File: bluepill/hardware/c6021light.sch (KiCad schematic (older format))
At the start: 77 parts, among them J1 Barrel_Jack_Switch, J10 Conn_01x02, J11 Conn_01x02, J12 XpressNet, J2 Conn_02x04_Odd_Even, J3 Conn_02x16_Row_Letter_First, J30 Loconet, J31 Conn_01x02, J32 Conn_01x02, J4 Conn_01x02, J5 Grove I2C, J50 USB_B_Micro, J51 Conn_01x06, J52 Debug UART, J6 Conn_01x02, J7 Conn_01x02, J8 RJ45, Q30 BC337, Q31 BC547, Q32 BC547, SW1 SW_Push, U1 L7805, U10 SN75176, U2 L7808, U3 MCP2562, U30 LM393, U4 ISO1050DUB, U50 CH340C

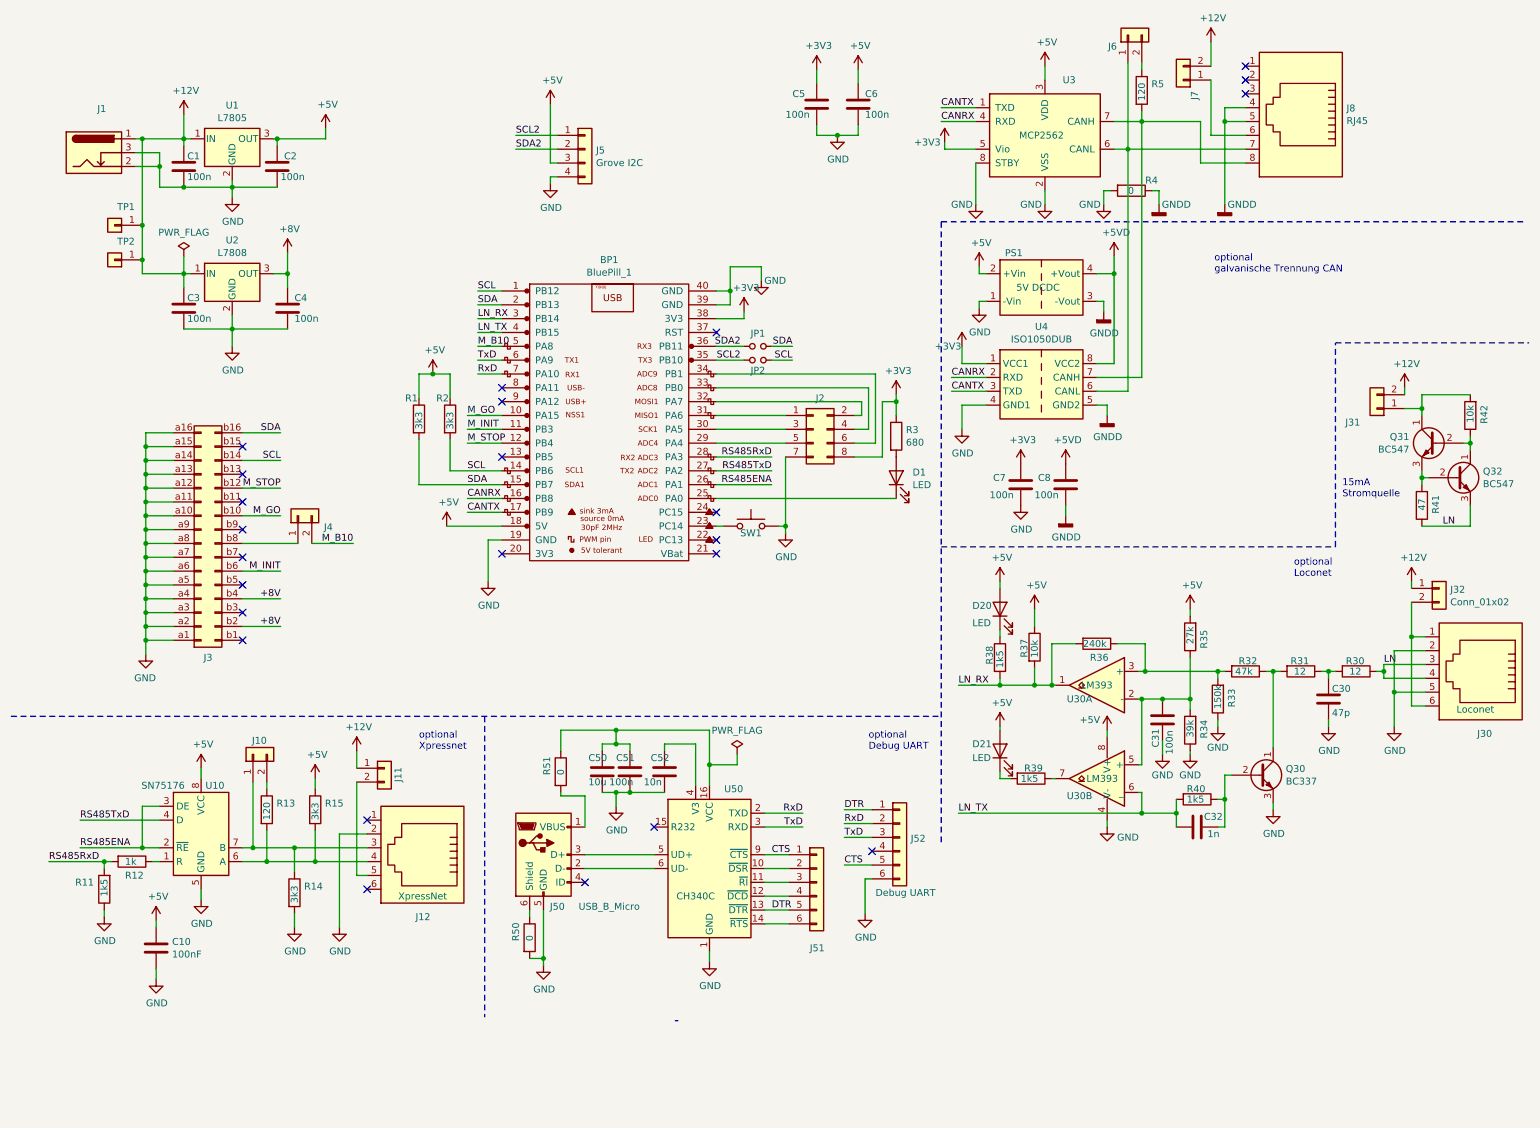
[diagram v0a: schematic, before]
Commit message: new PCB version 1.1. aka 2020/08 with some small fixes
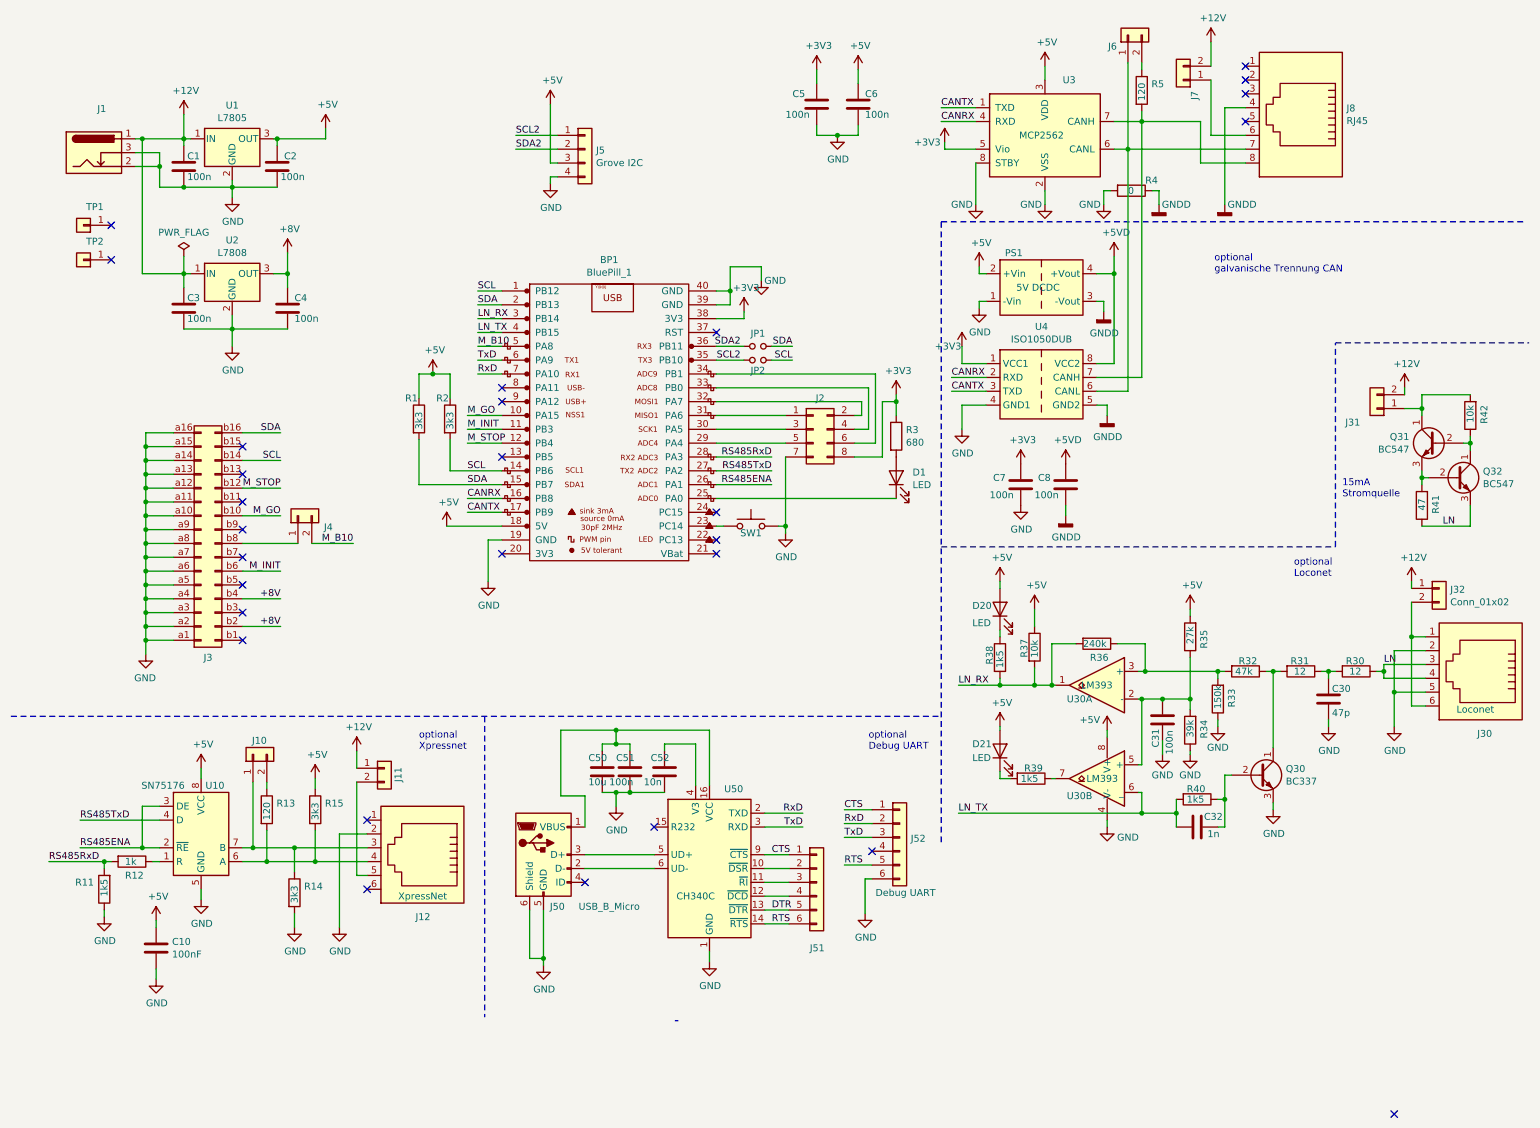
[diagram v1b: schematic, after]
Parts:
- removed R50, R51: 0, Resistor_SMD:R_1206_3216Metric_Pad1.42x1.75mm_HandSolder, symbol Device:R
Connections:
- net +12V: no longer TP1.1 (Pin_1), TP2.1 (Pin_1)
- net CTS: now also J52.1 (Pin_1); no longer J52.5 (Pin_5)
- net DTR: no longer J52.1 (Pin_1)
- net GND: now also J50.6 (Shield)
- net GNDD: no longer J8.5
- net RTS: now reaches J51.6 (Pin_6), U50.14 (~RTS)
- net RTS: now also J52.5 (Pin_5)
- net at C50.1, C51.1, U50.16 (VCC): now also J50.1 (VBUS)
- no-connect marks 24 -> 28
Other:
- moved on the sheet: TP1, TP2
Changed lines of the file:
@@
 Sheet 1 1
 Title "C6021 Light"
-Date "2020-06-09"
-Rev "1.0"
+Date "2020-08-03"
+Rev "1.1"
 Comp "Damian Philipp / Gerhard Bertelsmann"
 Comment1 ""
@@
 	7725 900  7725 1000
 $Comp
-L Connector:RJ45 J8
-U 1 1 5EDB2E8F
-P 9575 1200
-F 0 "J8" H 9245 1204 50  0000 R CNN
-F 1 "RJ45" H 9245 1295 50  0000 R CNN
-F 2 "w_conn_pc:mebp8" V 9575 1225 50  0001 C CNN
-F 3 "~" V 9575 1225 50  0001 C CNN
-	1    9575 1200
-	-1   0    0    1
-$EndComp
-$Comp
 L Device:C C5
 U 1 1 5EDB8D27
@@
 Wire Wire Line
 	9175 1200 9025 1200
-Wire Wire Line
-	9175 1300 9025 1300
 Wire Wire Line
 	9175 1400 8925 1400
@@
 Wire Wire Line
 	8175 5700 8175 5750
-$Comp
-L Device:R R50
-U 1 1 60480953
-P 4000 7200
-F 0 "R50" V 3900 7175 50  0000 L CNN
-F 1 "0" V 4000 7175 50  0000 L CNN
-F 2 "Resistor_SMD:R_1206_3216Metric_Pad1.42x1.75mm_HandSolder" V 3930 7200 50  0001 C CNN
-F 3 "~" H 4000 7200 50  0001 C CNN
-	1    4000 7200
-	1    0    0    -1
-$EndComp
 Wire Wire Line
 	4000 7350 4100 7350
@@
 Wire Wire Line
 	4100 7350 4100 7400
-Wire Wire Line
-	4000 7000 4000 7050
 $Comp
 L Device:C C51
@@
 Wire Wire Line
 	4625 5800 4625 5700
-Wire Wire Line
-	5300 5700 5300 5950
 Connection ~ 4625 5800
 Wire Wire Line
@@
 Wire Wire Line
 	5200 6100 5200 5800
-$Comp
-L Device:R R51
-U 1 1 6058F371
-P 4225 6000
-F 0 "R51" V 4125 5975 50  0000 L CNN
-F 1 "0" V 4225 5975 50  0000 L CNN
-F 2 "Resistor_SMD:R_1206_3216Metric_Pad1.42x1.75mm_HandSolder" V 4155 6000 50  0001 C CNN
-F 3 "~" H 4225 6000 50  0001 C CNN
-	1    4225 6000
-	1    0    0    -1
-$EndComp
-Wire Wire Line
-	4225 5850 4225 5700
 Wire Wire Line
 	4225 5700 4625 5700
@@
 Wire Wire Line
 	6475 6275 6275 6275
-Text Label 6275 6275 0    50   ~ 0
-DTR
 Wire Wire Line
 	6475 6675 6275 6675
-Text Label 6275 6675 0    50   ~ 0
-CTS
 NoConn ~ 6475 6575
 Wire Notes Line
@@
 	8925 1400 8925 1000
 Wire Wire Line
-	9025 1300 9025 1900
-Wire Wire Line
 	8325 1500 9175 1500
-Wire Wire Line
-	9025 1300 9025 1200
-Connection ~ 9025 1300
 Wire Notes Line
 	6975 2025 11200 2025
@@
 Text Notes 8950 2400 0    50   ~ 0
 optional\ngalvanische Trennung CAN
-Wire Wire Line
-	4225 6150 4225 6175
 Wire Wire Line
 	4225 6175 4400 6175
@@
 	1    0    0    -1
 $EndComp
-$Comp
-L power:PWR_FLAG #FLG0103
-U 1 1 60D33B68
-P 5500 5875
-F 0 "#FLG0103" H 5500 5950 50  0001 C CNN
-F 1 "PWR_FLAG" H 5500 6048 50  0000 C CNN
-F 2 "" H 5500 5875 50  0001 C CNN
-F 3 "~" H 5500 5875 50  0001 C CNN
-	1    5500 5875
-	1    0    0    -1
-$EndComp
-Wire Wire Line
-	5300 5950 5500 5950
-Wire Wire Line
-	5500 5950 5500 5875
-Connection ~ 5300 5950
-Wire Wire Line
-	5300 5950 5300 6100
 $Comp
 L Connector_Generic:Conn_01x04 J5
@@
 	1150 1425 1200 1425
 Wire Wire Line
-	1200 1425 1200 2050
-Wire Wire Line
 	1200 2400 1500 2400
 Connection ~ 1200 1425
@@
 Connection ~ 5850 4225
 $Comp
-L Connector_Generic:Conn_01x01 TP1
-U 1 1 5EE1214D
-P 1000 2050
-F 0 "TP1" H 918 1917 50  0000 C CNN
-F 1 "Conn_01x01" H 918 1916 50  0001 C CNN
-F 2 "TestPoint:Test_Point_NA" H 1000 2050 50  0001 C CNN
-F 3 "~" H 1000 2050 50  0001 C CNN
-	1    1000 2050
-	-1   0    0    1
-$EndComp
-Connection ~ 1200 2050
-Wire Wire Line
-	1200 2050 1200 2300
-$Comp
 L Connector_Generic:Conn_01x01 TP2
 U 1 1 5EE12B1B
-P 1000 2300
-F 0 "TP2" H 918 2167 50  0000 C CNN
-F 1 "Conn_01x01" H 918 2166 50  0001 C CNN
-F 2 "TestPoint:Test_Point_NA" H 1000 2300 50  0001 C CNN
-F 3 "~" H 1000 2300 50  0001 C CNN
-	1    1000 2300
+P 775 2300
+F 0 "TP2" H 693 2167 50  0000 C CNN
+F 1 "Conn_01x01" H 693 2166 50  0001 C CNN
+F 2 "TestPoint:Test_Point_NA" H 775 2300 50  0001 C CNN
+F 3 "~" H 775 2300 50  0001 C CNN
+	1    775  2300
 	-1   0    0    1
 $EndComp
-Connection ~ 1200 2300
-Wire Wire Line
-	1200 2300 1200 2400
 $Comp
 L Connector_Generic:Conn_02x04_Odd_Even J2
@@
 	10375 4775 10375 5025
 Connection ~ 10375 5025
+$Comp
+L Connector:RJ45 J8
+U 1 1 5EDB2E8F
+P 9575 1200
+F 0 "J8" H 9245 1204 50  0000 R CNN
+F 1 "RJ45" H 9245 1295 50  0000 R CNN
+F 2 "w_conn_pc:mebp8" V 9575 1225 50  0001 C CNN
+F 3 "~" V 9575 1225 50  0001 C CNN
+	1    9575 1200
+	-1   0    0    1
+$EndComp
+Wire Wire Line
+	9025 1200 9025 1900
+NoConn ~ 9175 1300
+NoConn ~ 10250 8475
+$Comp
+L Connector_Generic:Conn_01x01 TP1
+U 1 1 5EE1214D
+P 775 2050
+F 0 "TP1" H 693 1917 50  0000 C CNN
+F 1 "Conn_01x01" H 693 1916 50  0001 C CNN
+F 2 "TestPoint:Test_Point_NA" H 775 2050 50  0001 C CNN
+F 3 "~" H 775 2050 50  0001 C CNN
+	1    775  2050
+	-1   0    0    1
+$EndComp
+NoConn ~ 975  2050
+Wire Wire Line
+	1200 1425 1200 2400
+NoConn ~ 975  2300
+Wire Wire Line
+	4000 7000 4000 7350
+Wire Wire Line
+	4225 5700 4225 6175
+Wire Wire Line
+	5300 5700 5300 6100
+Text Label 5750 7100 0    50   ~ 0
+RTS
+Text Label 6275 6675 0    50   ~ 0
+RTS
+Text Label 6275 6275 0    50   ~ 0
+CTS
 $EndSCHEMATC
